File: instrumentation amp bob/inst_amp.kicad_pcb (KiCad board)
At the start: 2 copper layers, 30.5 x 20.3 mm, 26 parts, among them J1 Conn_01x03, J2 Conn_01x03, J3 Conn_01x05, U1 AD8429, U2 OP1177

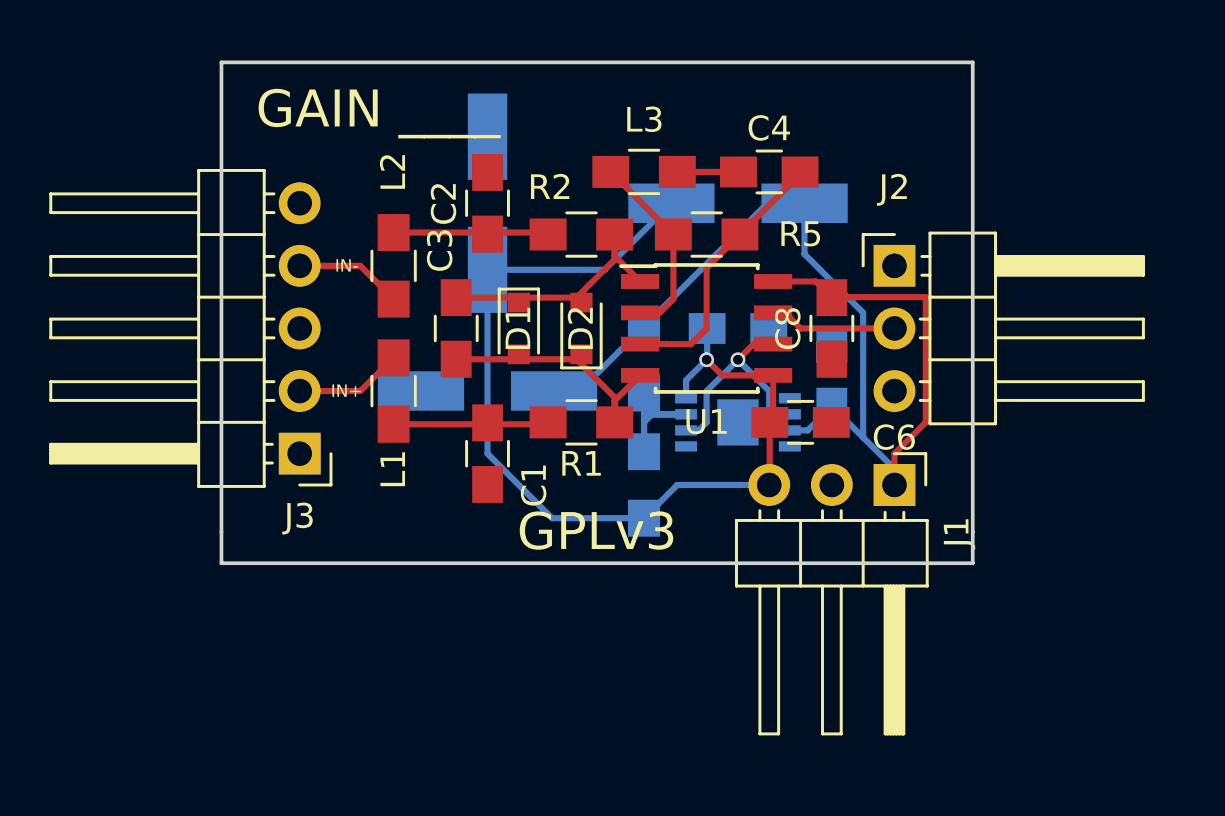
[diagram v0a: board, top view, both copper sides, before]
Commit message: incorporated review comments to layout
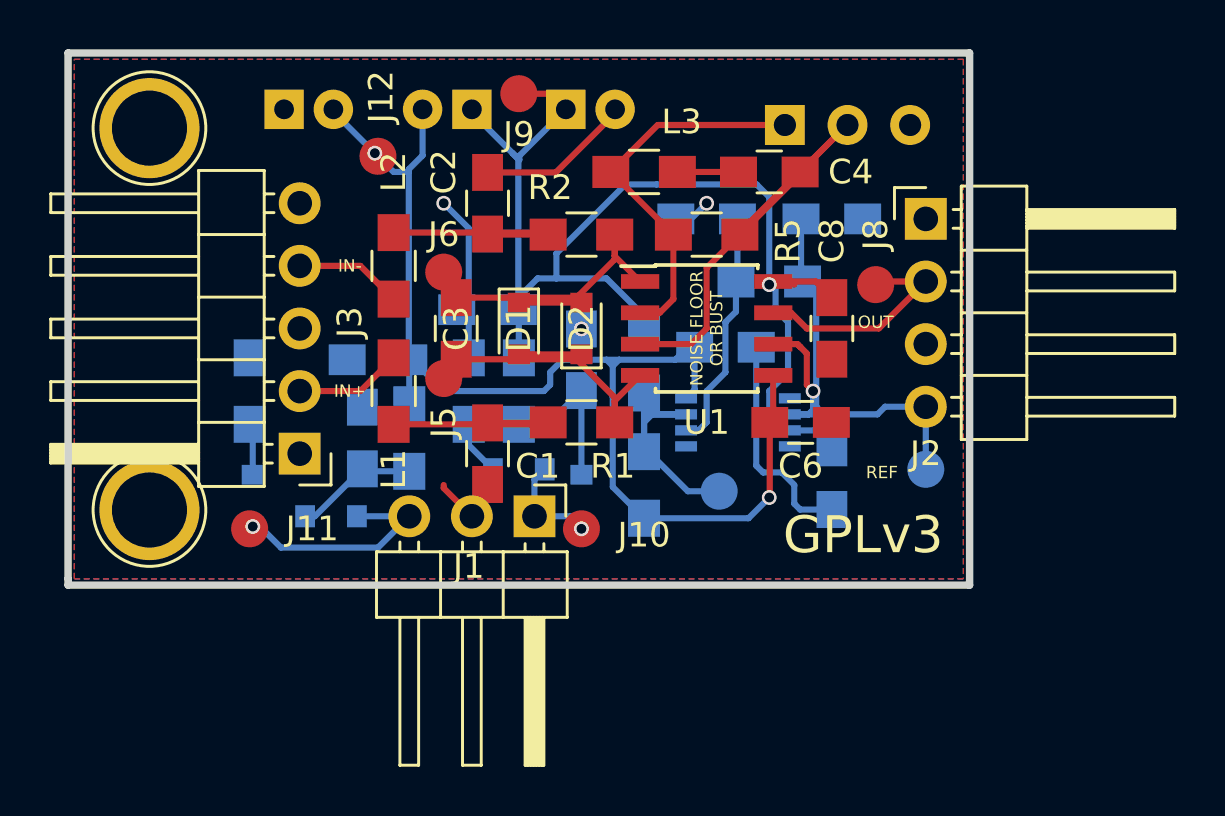
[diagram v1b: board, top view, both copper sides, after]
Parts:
- added C12: 0.1uF, Capacitors_SMD:C_0805_HandSoldering, B.Cu at (69.8, 117.3)
- added C13: 0.1uF, Capacitors_SMD:C_0805_HandSoldering, B.Cu at (73.7, 119.4)
- added C14: 0.1uF, Capacitors_SMD:C_0805_HandSoldering, B.Cu at (64.8, 122.6)
- added C15: 0.1uF, Capacitors_SMD:C_0805_HandSoldering, B.Cu at (65.4, 119.4)
- added C16: 0.1uF, Capacitors_SMD:C_0805_HandSoldering, B.Cu at (78.7, 113.7)
- added C17: 0.1uF, Capacitors_SMD:C_0805_HandSoldering, B.Cu at (83.8, 113.7)
- added D3: D, Diodes_SMD:D_0805, B.Cu at (73.7, 125.1)
- added D4: LED, Diodes_SMD:D_0805, B.Cu at (71.1, 123.8)
- added D5: LED, Diodes_SMD:D_0805, B.Cu at (60.3, 125.1)
- added D6: D, Diodes_SMD:D_0805, B.Cu at (63.5, 125.7)
- added J10: TEST_1P, Measurement_Points:Measurement_Point_Round-SMD-Pad_Small, F.Cu at (73.7, 126.2)
- added J11: TEST_1P, Measurement_Points:Measurement_Point_Round-SMD-Pad_Small, F.Cu at (60.2, 126.2)
- added J12: TEST_1P, Measurement_Points:Measurement_Point_Round-SMD-Pad_Small, F.Cu at (65.4, 111.1)
- added J4: TEST_1P, Measurement_Points:Measurement_Point_Round-SMD-Pad_Small, B.Cu at (79.2, 124.7)
- added J5: TEST_1P, Measurement_Points:Measurement_Point_Round-SMD-Pad_Small, F.Cu at (68.1, 120.1)
- added J6: TEST_1P, Measurement_Points:Measurement_Point_Round-SMD-Pad_Small, F.Cu at (68.1, 115.8)
- added J7: TEST_1P, Measurement_Points:Measurement_Point_Round-SMD-Pad_Small, B.Cu at (87.6, 123.8)
- added J8: TEST_1P, Measurement_Points:Measurement_Point_Round-SMD-Pad_Small, F.Cu at (85.6, 116.3)
- added J9: TEST_1P, Measurement_Points:Measurement_Point_Round-SMD-Pad_Small, F.Cu at (71.1, 108.6)
- added L4: 10uH, Inductors_SMD:L_0805_HandSoldering, B.Cu at (71.1, 120.7)
- added L5: 10uH, Inductors_SMD:L_0805_HandSoldering, B.Cu at (66.7, 122.6)
- added L6: L, Inductors_SMD:L_0805_HandSoldering, B.Cu at (81.3, 116.2)
- added R6: R, Resistors_SMD:R_0805_HandSoldering, B.Cu at (69.1, 120.7)
- added R7: R, Resistors_SMD:R_0805_HandSoldering, B.Cu at (60.2, 120.7)
- added REF**: 1pin, Connectors:1pin, F.Cu at (56.1, 125.5)
- added REF**: 1pin, Connectors:1pin, F.Cu at (56.1, 110.0)
- added RV1: POT, Potentiometers:Potentiometer_Trimmer_Bourns_PV36W, B.Cu at (81.9, 109.9)
- C10, C11, C9: footprint Capacitors_SMD:CP_Elec_6.3x7.7 -> Capacitors_THT:CP_Radial_D5.0mm_P2.00mm
- J2: value Conn_01x03 -> Conn_01x04; footprint Pin_Headers:Pin_Header_Angled_1x03_Pitch2.54mm -> Pin_Headers:Pin_Header_Angled_1x04_Pitch2.54mm
- moved J1 14.7 mm to (71.8, 125.7)
- moved C9 11.9 mm to (73.0, 109.2), turned to 0 degrees
- moved C10 11.4 mm to (69.2, 109.2)
- moved C11 9.09 mm to (61.6, 109.2), turned to 0 degrees
- moved C5 4.19 mm to (83.8, 124.2), turned to 90 degrees
- moved J2 2.29 mm to (87.6, 113.7)
- moved C7 0.92 mm to (79.5, 118.9)
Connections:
- J1 pad 1: +5V -> Net-(D3-Pad2)
- J1 pad 3: -5V -> Net-(D5-Pad2)
- U2 pad 2: REF -> Net-(C16-Pad1)
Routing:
- net GND: track 0.38 -> 26.9 mm, vias 0 -> 3
- net REF: track 9.12 -> 22.3 mm
- net -5V: track 39.8 -> 50.0 mm, vias 1 -> 2
- net Net-(C16-Pad1): track 0.00 -> 9.66 mm
- net Net-(D5-Pad2): track 0.00 -> 9.52 mm, vias 0 -> 1
- net Net-(C4-Pad2): track 10.9 -> 19.9 mm
- net Net-(L3-Pad1): track 7.79 -> 15.6 mm
- net Net-(C13-Pad1): track 0.00 -> 6.52 mm
- net +5V: track 44.8 -> 50.9 mm, vias 0 -> 1
- net Net-(C14-Pad1): track 0.00 -> 4.98 mm
- net Net-(D3-Pad2): track 0.00 -> 4.25 mm, vias 0 -> 1
- net OUT: track 5.18 -> 9.33 mm
- net Net-(C3-Pad1): track 10.4 -> 14.2 mm
- net Net-(J4-Pad1): track 7.80 -> 11.5 mm
- net Net-(C3-Pad2): track 10.4 -> 13.9 mm
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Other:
- board size 30.5 x 20.3 mm -> 36.6 x 21.6 mm
- board text added: "+5V"
- board text added: "-5V"
- board text added: "AD8428 ☐ AD8429 ☐ VER 001"
- board text added: "OUT"
- board text added: "REF"
- board text added: "REF V____ GAIN ____"
- board text removed: "AD8428 ☐ AD8429 ☐"
- board text removed: "GAIN ____"
- board text removed: "REF VOLTAGE ____"
